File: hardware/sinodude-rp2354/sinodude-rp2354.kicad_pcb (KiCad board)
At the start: 2 copper layers, 64 x 36 mm, 93 parts, among them J1 USB-C, J2 SWD TC2030-IDC latching, J4 DUT, Q1 2N7002, SW1 BOOTSEL, SW2 RESET, U1 RP2354A, U2 AMS1117-3.3, U3 TPS2114APW, U4 SN74LVC8T245PW, U5 SN74LVC1T45DBV, U6 SN74LVC1T45DBV, Y1 12MHz/CL10pF/ESR50R/ABM8-272-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

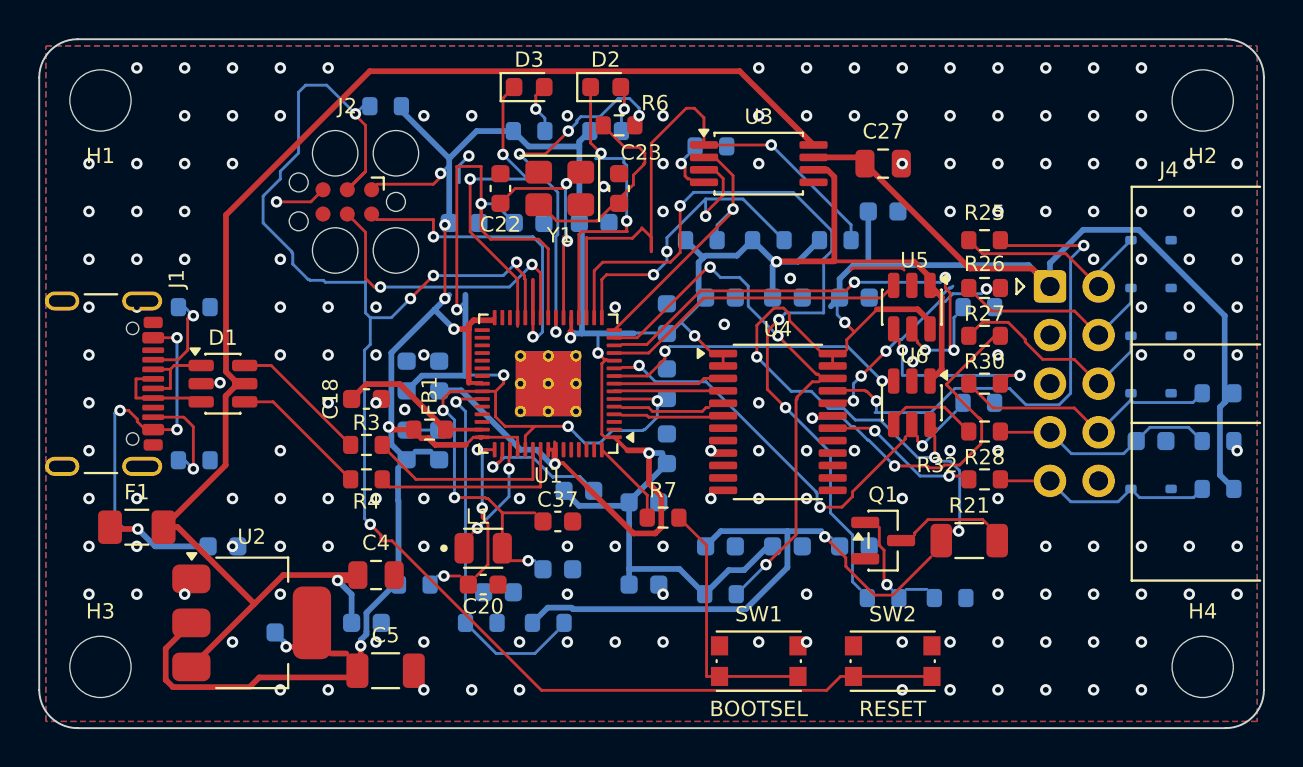
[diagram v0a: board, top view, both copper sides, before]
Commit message: hardware: land every track in the middle of its pad, and finish the staircases
TMS_3V3 was the visible case: at U4 pin 5 the track centreline ran entirely
outside the pad and only a corner of the end cap overlapped it. DRC calls that
connected because copper touches copper. It is a real joint on the gerbers and
a coin toss on the bench.

It was not one track. Measuring how far each terminating track actually
penetrates the pad it lands on found 82 ends under 0.1 mm, 31 of them at zero,
spread across every net. The rule now is that a terminating track ends at the
pad centre, so the full track width sits on pad copper.

Two things had to be got right before the fix was safe. Deciding whether an
end is a pad terminus has to be geometric, not a lookup on exact coordinates:
two tracks that meet by overlapping rather than by sharing a vertex look like
two termini, and rerouting one of them breaks the joint. And a segment whose
both ends need landing is one job, pad centre to pad centre, not two.

The check that matters is per pad, not per track, because a pad can be left
hanging by a chain whose last link looks fine on its own. Nine pads were still
weak after the per-track pass, two with no track overlap at all, and those get
an additive spur from the nearest same-net track into the pad centre - adding
copper cannot break what is already connected.

Also finished the staircase work from the last commit with the same
convergence loop. Three chains remain that have no clean path clearing their
neighbours.

823 segments. DRC and ERC clean at every severity, nothing unconnected, no pad
attached by less than half a track width, GND still one region, every track on
0, 45 or 90 degrees.
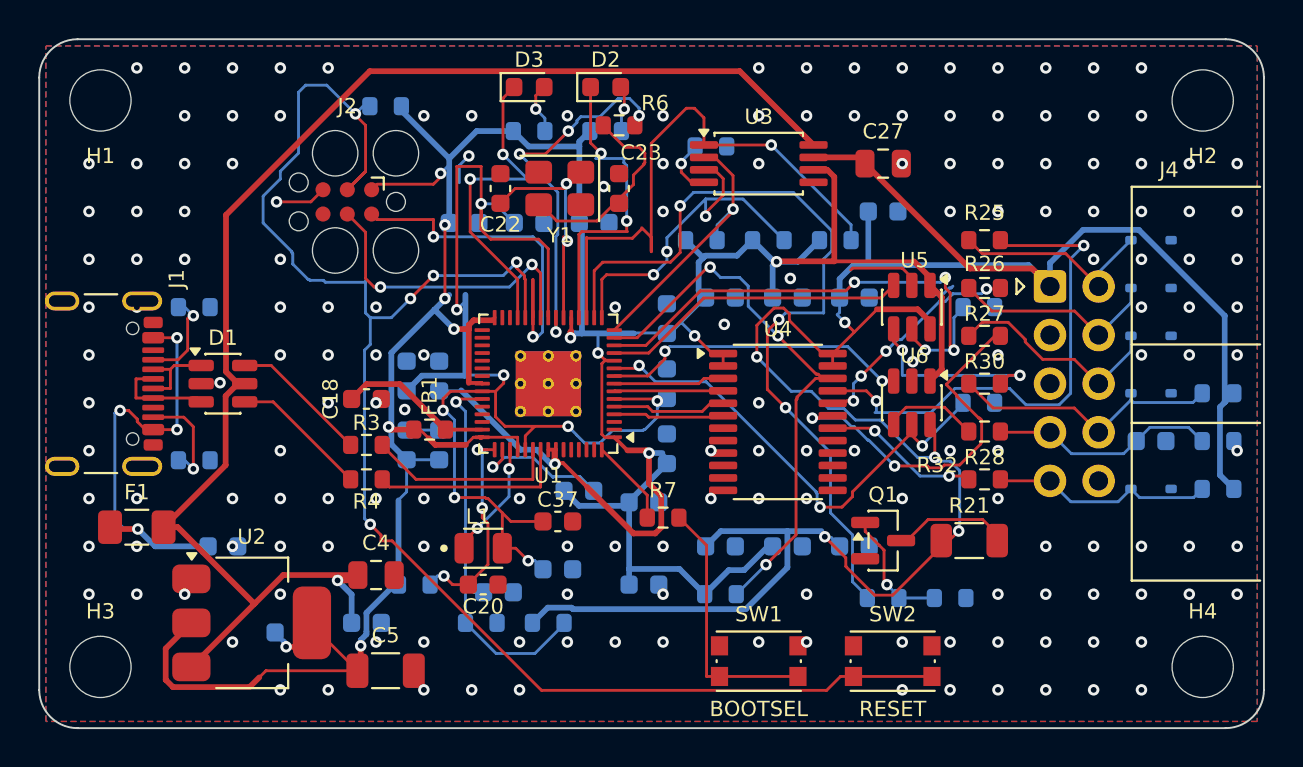
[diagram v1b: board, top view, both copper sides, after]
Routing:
- net +3V3: track 181.1 -> 189.0 mm
- net VTGT: track 118.9 -> 122.8 mm
- net +1V1: track 64.9 -> 68.4 mm
- net KEY_DIR: track 23.2 -> 25.7 mm
- net GND: track 16.4 -> 18.4 mm
- net VREG_AVDD: track 9.69 -> 11.5 mm
- net Net-(Q1-D): track 4.29 -> 6.13 mm
- net DATA_DIR: track 26.3 -> 28.1 mm
- net XLAT_OE: track 28.3 -> 29.9 mm
- net Net-(U3-ILIM): track 1.64 -> 3.06 mm
- net VREG_LX: track 4.74 -> 6.14 mm
- net Net-(Q1-G): track 4.62 -> 5.93 mm
- net TMS_3V3: track 4.72 -> 5.97 mm
- net VTGT_SENSE: track 19.6 -> 20.8 mm
- net NRST_3V3: track 4.59 -> 5.78 mm
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
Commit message: hardware: simplify whole paths, weld hairline joins, restore power track widths
Three faults, one of them mine.

The jaggedness left on TMS_B was not a staircase, so the chain-based pass
could not see it. Simplification now works on whole paths: each route between
its anchors is walked and the longest span that can be replaced by a clean
45 degree pair is taken, greedily, checked against every foreign pad, track
and via at the real clearance. That removes doglegs and unmitred corners as
well as staircases. 823 segments to 714 for the same routing.

TMS_B's sharp corner by R30 turned out to be two segments meeting 0.024 mm
apart rather than at a vertex - a hairline joint, and the reason the path
walker saw two paths instead of one. Welding those onto the intersection of
their two lines keeps both angles exactly on 45, which naive snapping does
not: an earlier attempt at that broke 24 angles and was reverted. 19 clusters
welded; the rest are left alone because no single point preserves every angle
meeting there. Every track end now overlaps its joint by at least 0.05 mm
except four GND ends, which the pour covers anyway.

The thin power traces were my own doing. The cleanup scripts wrote new
segments at a hardcoded 0.15 mm, so every power net they touched came out at
signal width. They carry the original width through now, and a separate pass
walks every Power-class segment back up to 0.30 mm, stepping down only where
a neighbour blocks it. 269 of 331 power segments are at full class width.

The V detour on TMS_B stays: R30's pad and the D8 net sit across the direct
line, so the way round is real.

DRC and ERC clean at every severity, nothing unconnected, every pad attached
by at least half a track width, GND one region, all tracks on 0, 45 or 90.
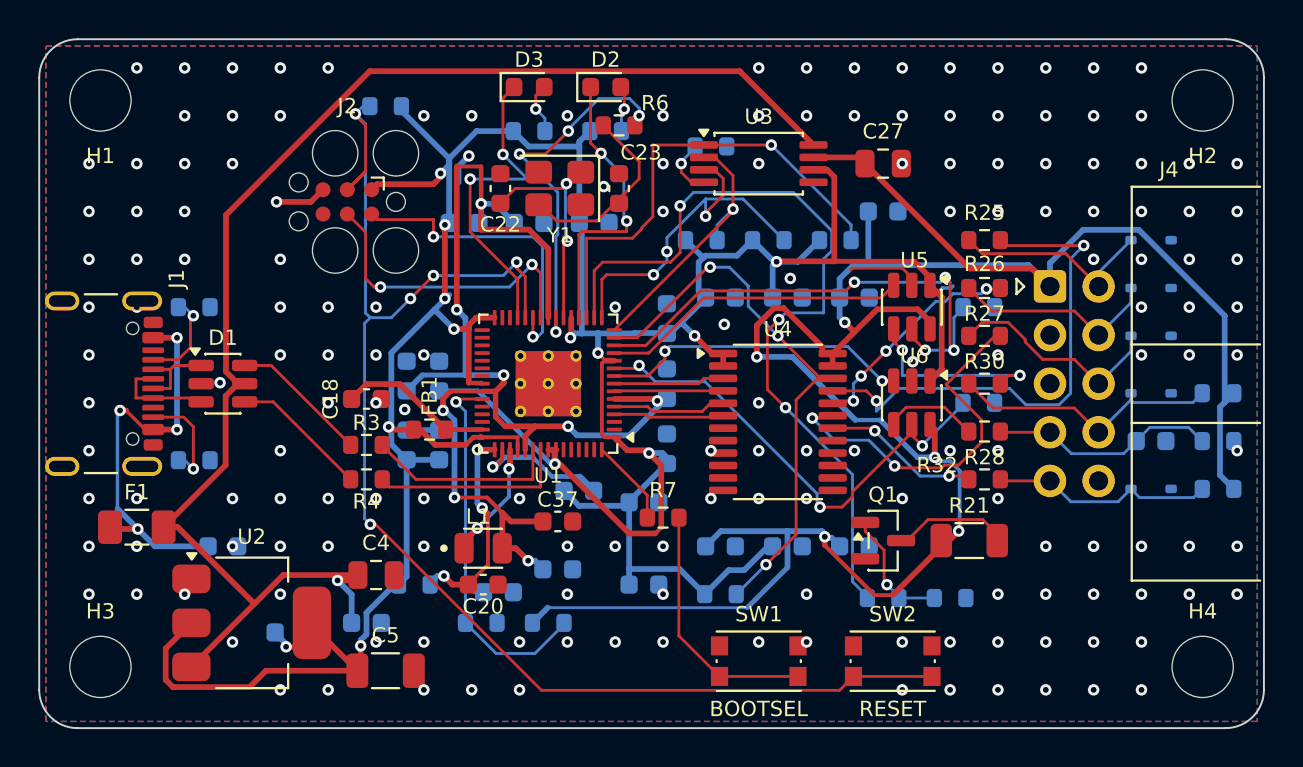
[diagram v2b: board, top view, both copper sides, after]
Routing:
- net RUN: track 83.6 -> 74.0 mm
- net VTGT_STAT: track 29.8 -> 24.7 mm
- net SWDIO: track 20.2 -> 16.2 mm
- net +1V1: track 68.4 -> 66.2 mm
- net LED_ACT: track 16.4 -> 15.2 mm
- net Net-(C23-Pad1): track 10.8 -> 10.1 mm
- net VBUS: track 22.3 -> 21.7 mm
- net VREG_AVDD: track 11.5 -> 11.0 mm

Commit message: hardware: chamfer every right angle into two 45 degree turns
You were right that the TMS_B corner could be two 45s. Backing off along each
leg by the same distance and joining the two points gives a segment that is
axis-aligned when the legs are diagonal and diagonal when they are
axis-aligned, so one 90 degree turn becomes two 45s either way, and the
chamfer always cuts toward the inside of the corner - away from whatever the
corner was avoiding.

18 right angles on the board, all gone. The chamfer is taken as wide as
clearance allows, stepping down from 45% of the shorter leg.

The TMS_B one needed a fix to the checker first. It was rejecting the chamfer
because the outgoing leg sits 0.108 mm from R30's pad by my measure, under the
0.15 mm rule - except KiCad passes it, because the pad is a roundrect and my
check uses its bounding box, which overstates the pad at the corners. The leg
was pre-existing and unchanged by the chamfer; shortening a segment cannot
make its clearance worse, so the legs are no longer re-checked at all.

731 segments. DRC and ERC clean at every severity, nothing unconnected, no
right angles, every track on 0, 45 or 90, every pad attached by at least half
a track width, 273 of 336 power segments at full class width, GND one region.
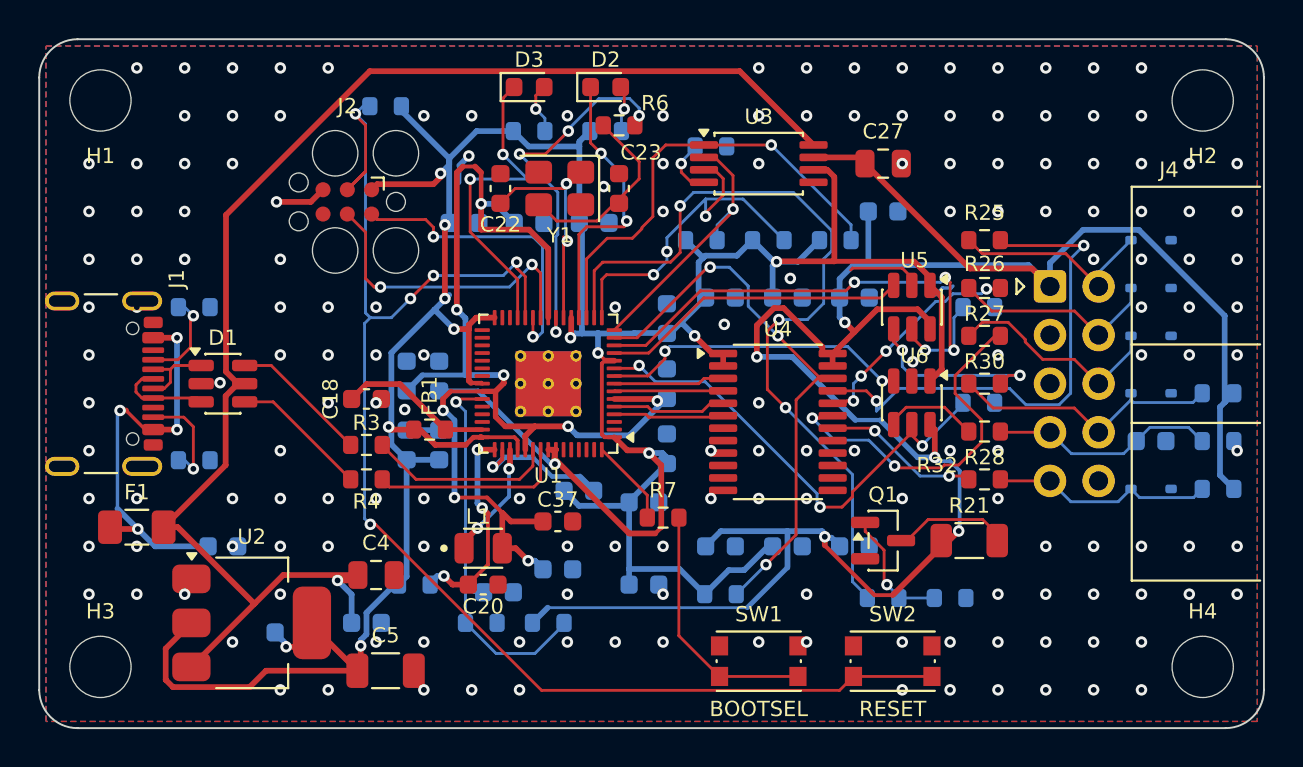
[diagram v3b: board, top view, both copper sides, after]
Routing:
- net VTGT_STAT: track 24.7 -> 23.7 mm

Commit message: hardware: tighten the core regulator and crystal layout
The switching regulator block was laid out with its parts several
millimetres from the pins they serve, against the RP2350 guide's note
that this block's layout is critical.

- L1 moves under U1's south row: VREG_LX drops from 6.1 mm to 3.5 mm and
  now runs straight down from pin 48, threading the 0.60 mm gap between
  the pin 47 and pin 49 pads at 0.25 mm.
- C21 moves to F.Cu beside L1's output, so the L to C_OUT link is 1.6 mm
  on one layer instead of 2.4 mm across a via.
- C20 moves under pin 46: the VREG_AVDD filter cap is 3.8 mm from the
  pin rather than 7.2 mm.
- C19 moves from 9.2 mm to 5.2 mm of U1's VREG_VIN pin.
- C37 was 2.5 mm from C21, where it just doubled the 4.7 uF the
  regulator is compensated for. It now sits at DVDD pin 39, 12.5 mm of
  copper from C21.
- Y1 is rotated so XIN lands on the crystal terminal nearest U1: XIN is
  8.5 mm on F.Cu with no vias, down from 12.4 mm across two.

Pin 47 carries the switching return and now drops straight into the
pour through its own via instead of sharing a track.

DRC and ERC clean at every severity, no unconnected items, no
schematic parity errors, every track on 0/45/90, every pad entered at
its centre, every Power-class track at its netclass width.
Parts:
- C21: moved to F.Cu
- moved C37 12.3 mm to (136.3, 102.3), turned to 180 degrees
- moved C19 6.39 mm to (142.0, 113.6)
- moved C20 3.77 mm to (138.3, 112.0), turned to 180 degrees
- moved C21 3.08 mm to (145.4, 112.2)
- moved L1 2.69 mm to (142.0, 112.2)
- turned Y1 to 0 degrees
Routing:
- net +3V3: track 188.8 -> 178.9 mm
- net +1V1: track 65.9 -> 61.3 mm, vias 8 -> 7
- net XIN: track 12.4 -> 8.54 mm, vias 2 -> 0
- net VREG_AVDD: track 11.0 -> 7.74 mm
- net GND: track 18.3 -> 15.4 mm, vias 169 -> 168
- net VREG_LX: track 6.14 -> 3.45 mm
- net RUN: track 74.0 -> 72.7 mm
- net XOUT: track 19.0 -> 20.1 mm
- net Net-(C23-Pad1): track 10.1 -> 9.74 mm, vias 0 -> 2

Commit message: hardware: name header pin 7 TDA, not KEY
SinoWealth's tool-selection note tabulates adapter signals per target
core: ARM gets SWD (VDD SWCLK SWDIO GND), Andes gets AICE
(VDD TCK TDA GND), and the 8051 parts get VDD TCK TDI TDO GND. The 2x5
header carries both styles at once, so pin 7 is the Andes AICE data
wire sharing TCK with the 8051 path. It was carried over from SinoLink
as an unexplained "KEY" line.

Renames KEY_3V3, KEY_B and KEY_DIR to TDA_3V3, TDA_B and TDA_DIR.

Also corrects the GPIO map, which had DATA and KEY on each other's
translators and implied GPIO2 was TCK. The schematic wires GPIO2-5 to
nRST, TMS, TDI, TCK in that order, GPIO6/7 to U6 and GPIO8/9 to U5.
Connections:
- net KEY_3V3 renamed TDA_3V3
- net KEY_B renamed TDA_B
- net KEY_DIR renamed TDA_DIR
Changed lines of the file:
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@@
 			(layers "F.Cu" "F.Mask" "F.Paste")
 			(roundrect_rratio 0.25)
-			(net "KEY_3V3")
+			(net "TDA_3V3")
 		)
 		(pad "10" smd roundrect
@@
 			(layers "F.Cu" "F.Mask" "F.Paste")
 			(roundrect_rratio 0.25)
-			(net "KEY_DIR")
+			(net "TDA_DIR")
 		)
 		(pad "11" smd roundrect
@@
 			(layers "F.Cu" "F.Mask" "F.Paste")
 			(roundrect_rratio 0.25)
-			(net "KEY_B")
+			(net "TDA_B")
 		)
 		(pad "2" smd roundrect
@@
 			(layers "F.Cu" "F.Mask" "F.Paste")
 			(roundrect_rratio 0.25)
-			(net "KEY_3V3")
+			(net "TDA_3V3")
 		)
 		(pad "4" smd roundrect
@@
 			(layers "F.Cu" "F.Mask" "F.Paste")
 			(roundrect_rratio 0.25)
-			(net "KEY_B")
+			(net "TDA_B")
 		)
 		(pad "5" smd roundrect
@@
 			(layers "F.Cu" "F.Mask" "F.Paste")
 			(roundrect_rratio 0.25)
-			(net "KEY_DIR")
+			(net "TDA_DIR")
 		)
 		(pad "6" smd roundrect
@@
 			(layers "B.Cu" "B.Mask" "B.Paste")
 			(roundrect_rratio 0.25)
-			(net "KEY_DIR")
+			(net "TDA_DIR")
 		)
 		(pad "2" smd roundrect
@@
 		(width 0.15)
 		(layer "F.Cu")
-		(net "KEY_3V3")
+		(net "TDA_3V3")
 	)
 	(segment
@@
 		(width 0.15)
 		(layer "F.Cu")
-		(net "KEY_3V3")
+		(net "TDA_3V3")
 	)
 	(segment
@@
 		(width 0.15)
 		(layer "F.Cu")
-		(net "KEY_3V3")
+		(net "TDA_3V3")
 	)
 	(segment
@@
 		(width 0.15)
 		(layer "F.Cu")
-		(net "KEY_3V3")
+		(net "TDA_3V3")
 	)
 	(via
@@
 		(drill 0.3)
 		(layers "F.Cu" "B.Cu")
-		(net "KEY_3V3")
+		(net "TDA_3V3")
 	)
 	(via
@@
 		(drill 0.3)
 		(layers "F.Cu" "B.Cu")
-		(net "KEY_3V3")
+		(net "TDA_3V3")
 	)
 	(segment
@@
 		(width 0.15)
 		(layer "B.Cu")
-		(net "KEY_3V3")
+		(net "TDA_3V3")
 	)
 	(segment
@@
 		(width 0.15)
 		(layer "B.Cu")
-		(net "KEY_3V3")
+		(net "TDA_3V3")
 	)
 	(segment
@@
 		(width 0.15)
 		(layer "B.Cu")
-		(net "KEY_3V3")
+		(net "TDA_3V3")
 	)
 	(segment
@@
 		(width 0.15)
 		(layer "F.Cu")
-		(net "KEY_DIR")
+		(net "TDA_DIR")
 	)
 	(segment
@@
 		(width 0.15)
 		(layer "F.Cu")
-		(net "KEY_DIR")
+		(net "TDA_DIR")
 	)
 	(segment
@@
 		(width 0.15)
 		(layer "F.Cu")
-		(net "KEY_DIR")
+		(net "TDA_DIR")
 	)
 	(segment
@@
 		(width 0.15)
 		(layer "F.Cu")
-		(net "KEY_DIR")
+		(net "TDA_DIR")
 	)
 	(segment
@@
 		(width 0.15)
 		(layer "F.Cu")
-		(net "KEY_DIR")
+		(net "TDA_DIR")
 	)
 	(segment
@@
 		(width 0.15)
 		(layer "F.Cu")
-		(net "KEY_DIR")
+		(net "TDA_DIR")
 	)
 	(segment
@@
 		(width 0.15)
 		(layer "F.Cu")
-		(net "KEY_DIR")
+		(net "TDA_DIR")
 	)
 	(segment
@@
 		(width 0.15)
 		(layer "F.Cu")
-		(net "KEY_DIR")
+		(net "TDA_DIR")
 	)
 	(segment
@@
 		(width 0.15)
 		(layer "F.Cu")
-		(net "KEY_DIR")
+		(net "TDA_DIR")
 	)
 	(via
@@
 		(drill 0.3)
 		(layers "F.Cu" "B.Cu")
-		(net "KEY_DIR")
+		(net "TDA_DIR")
 	)
 	(via
@@
 		(drill 0.3)
 		(layers "F.Cu" "B.Cu")
-		(net "KEY_DIR")
+		(net "TDA_DIR")
 	)
 	(via
@@
 		(drill 0.3)
 		(layers "F.Cu" "B.Cu")
-		(net "KEY_DIR")
+		(net "TDA_DIR")
 	)
 	(segment
@@
 		(width 0.15)
 		(layer "B.Cu")
-		(net "KEY_DIR")
+		(net "TDA_DIR")
 	)
 	(segment
@@
 		(width 0.15)
 		(layer "B.Cu")
-		(net "KEY_DIR")
+		(net "TDA_DIR")
 	)
 	(segment
@@
 		(width 0.15)
 		(layer "B.Cu")
-		(net "KEY_DIR")
+		(net "TDA_DIR")
 	)
 	(segment
@@
 		(width 0.15)
 		(layer "B.Cu")
-		(net "KEY_DIR")
+		(net "TDA_DIR")
 	)
 	(segment
@@
 		(width 0.15)
 		(layer "B.Cu")
-		(net "KEY_DIR")
+		(net "TDA_DIR")
 	)
 	(segment
@@
 		(width 0.15)
 		(layer "B.Cu")
-		(net "KEY_DIR")
+		(net "TDA_DIR")
 	)
 	(segment
@@
 		(width 0.15)
 		(layer "B.Cu")
-		(net "KEY_DIR")
+		(net "TDA_DIR")
 	)
 	(segment
@@
 		(width 0.15)
 		(layer "B.Cu")
-		(net "KEY_DIR")
+		(net "TDA_DIR")
 	)
 	(segment
@@
 		(width 0.15)
 		(layer "F.Cu")
-		(net "KEY_B")
+		(net "TDA_B")
 	)
 	(segment
@@
 		(width 0.15)
 		(layer "F.Cu")
-		(net "KEY_B")
+		(net "TDA_B")
 	)
 	(segment
@@
 		(width 0.15)
 		(layer "F.Cu")
-		(net "KEY_B")
+		(net "TDA_B")
 	)
 	(segment
@@
 		(width 0.15)
 		(layer "F.Cu")
-		(net "KEY_B")
+		(net "TDA_B")
 	)
 	(segment

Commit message: hardware: make TDA a working data line
Header pin 7 carried a 330 R series resistor and a fitted 100 nF to
ground, a 33 us low-pass on a wire whose whole protocol is edge timing,
plus a 10 k pull-down where the other two bidirectional lines pull up,
and it was the only target signal with no ESD clamp.

Those passives came from reading SinoLink's DUT sheet wrong. Neither is
on SinoLink's TDA: its cap position C28 carries the value DNI and is not
fitted, and the only 330 R on that sheet is a transistor-switched
pull-up on TDO, a different pin. SinoLink does clamp TDA, with D9.

So pin 7 now matches nRST and DATA exactly:

- C36 deleted; D9 (H5VSD3B) takes its footprint, keeping the D7/D8/D9
  clamp row aligned
- R32 330 R to 22 R, the value every other target line uses
- R33 repointed from GND to VTGT, matching R29 and R31
- the GND stitching via that touched R33's far pad moved 1 mm clear,
  now that the pad is no longer ground

DRC and ERC clean at every severity, no unconnected items, no schematic
parity errors, 88 placed parts unchanged, every track still on 0/45/90
with every pad entered at its centre.
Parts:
- removed C36: 100nF, Capacitor_SMD:C_0603_1608Metric
- added D9: H5VSD3B/VRWM5V/SOD-323, Diode_SMD:D_SOD-323, B.Cu at (174.6, 108.0)
- R32: value 330R -> 22R
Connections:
- R33 pad 2: GND -> VTGT
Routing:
- net Net-(D9-A1): track 11.9 -> 14.0 mm
- net VTGT: track 122.6 -> 123.7 mm
